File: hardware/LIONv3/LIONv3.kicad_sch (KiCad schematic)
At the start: 41 parts, among them SW1 RESET, SW2 BOOT, U1 TCAN3414DR, U14 UART, U15 I2C, U16 CAN, U17 PWR_3V3, U18 PWR_5V, U19 PWR_GND, U2 TYPE-C_16PIN_2MD(073), U3 ESP32-C6-MINI-1-N4, U4 TMP112AIDRLR

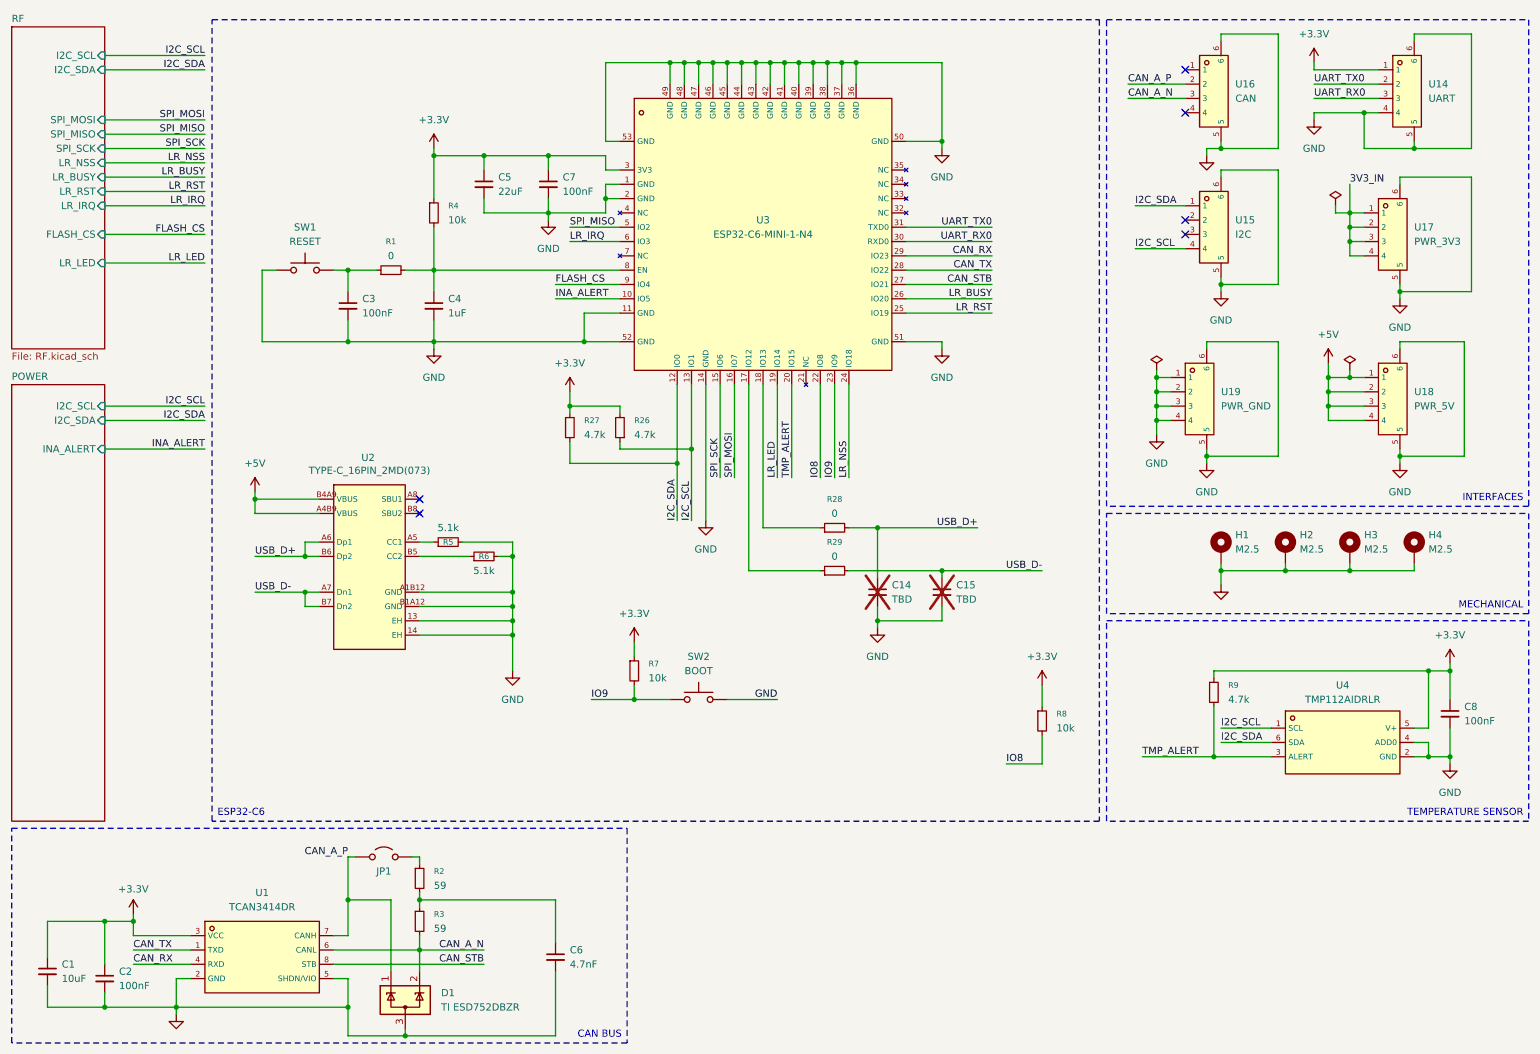
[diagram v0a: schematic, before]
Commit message: feat(hardware): add final components position
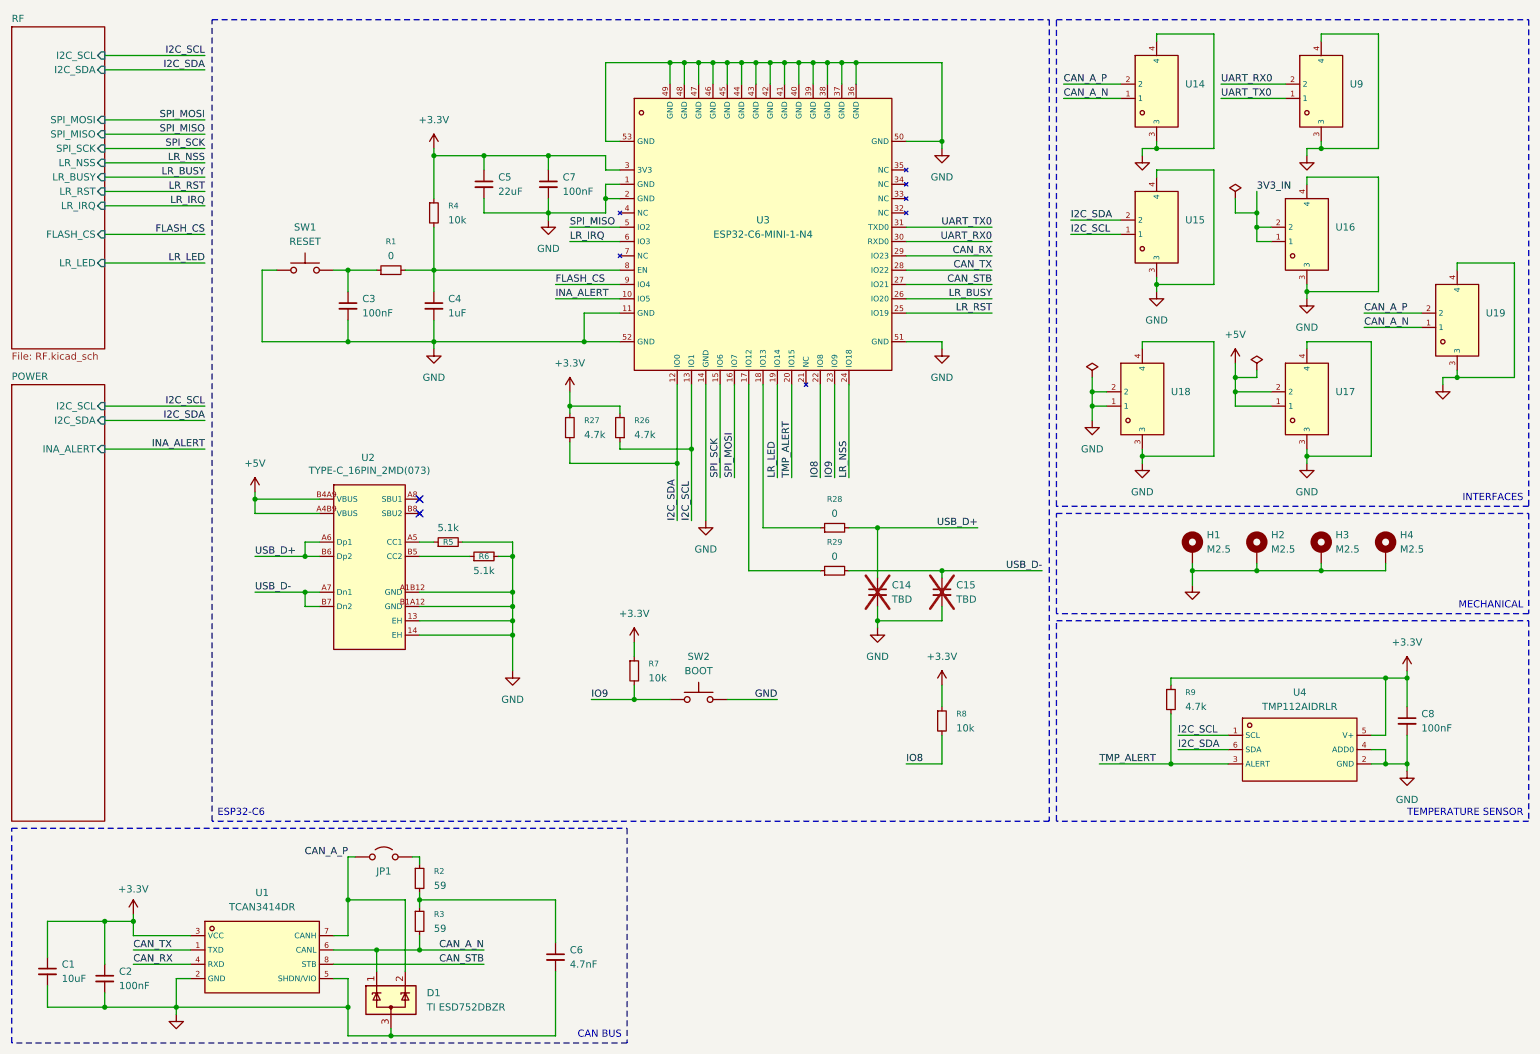
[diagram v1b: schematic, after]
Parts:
- removed U14: UART, LIONv3-Footprints:CONN-SMD_4P-P1.25_53261-0471, symbol LIONv3-Symbols:532610471_C696092
- removed U15: I2C, LIONv3-Footprints:CONN-SMD_4P-P1.25_53261-0471, symbol LIONv3-Symbols:532610471_C696092
- removed U16: CAN, LIONv3-Footprints:CONN-SMD_4P-P1.25_53261-0471, symbol LIONv3-Symbols:532610471_C696092
- removed U17: PWR_3V3, LIONv3-Footprints:CONN-SMD_4P-P1.25_53261-0471, symbol LIONv3-Symbols:532610471_C696092
- removed U18: PWR_5V, LIONv3-Footprints:CONN-SMD_4P-P1.25_53261-0471, symbol LIONv3-Symbols:532610471_C696092
- removed U19: PWR_GND, LIONv3-Footprints:CONN-SMD_4P-P1.25_53261-0471, symbol LIONv3-Symbols:532610471_C696092
- added U14, U15, U16, U17, U18, U19, U9: HC-1_25-2PWT, LIONv3-Footprints:CONN-SMD_2P-P1.25-HC-1.25-2PWT, symbol LIONv3-Symbols:HC-1_25-2PWT
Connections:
- net +5V: now also U17.1, U17.2
- net 3V3_IN: now also U16.1, U16.2
- net CAN_A_N: now also D1.1 (K), U14.1, U19.1; no longer D1.2 (K)
- net CAN_A_P: now also D1.2 (K), U14.2, U19.2; no longer D1.1 (K)
- net GND: now also U14.3, U14.4, U15.3, U15.4, U16.3, U16.4, U17.3, U17.4, U18.1, U18.2, U18.3, U18.4, U19.3, U19.4, U9.3, U9.4
- net I2C_SCL: now also U15.1
- net I2C_SDA: now also U15.2
- net UART_RX0: now also U9.2
- net UART_TX0: now also U9.1
- no-connect marks 6 -> 2
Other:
- moved on the sheet: C8, D1, H1, H2, H3, H4, R8, R9, U4

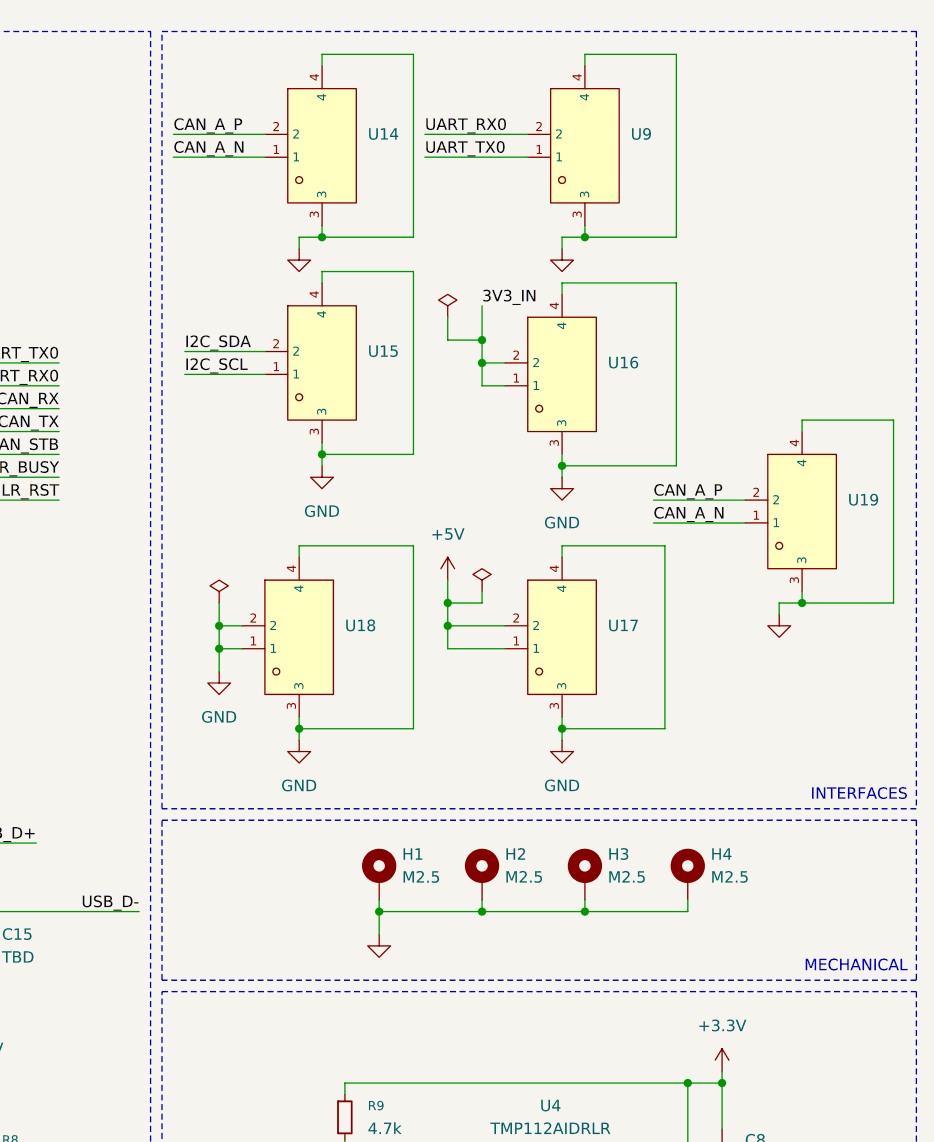
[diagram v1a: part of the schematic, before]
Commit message: feat(hardware): organize repo structure
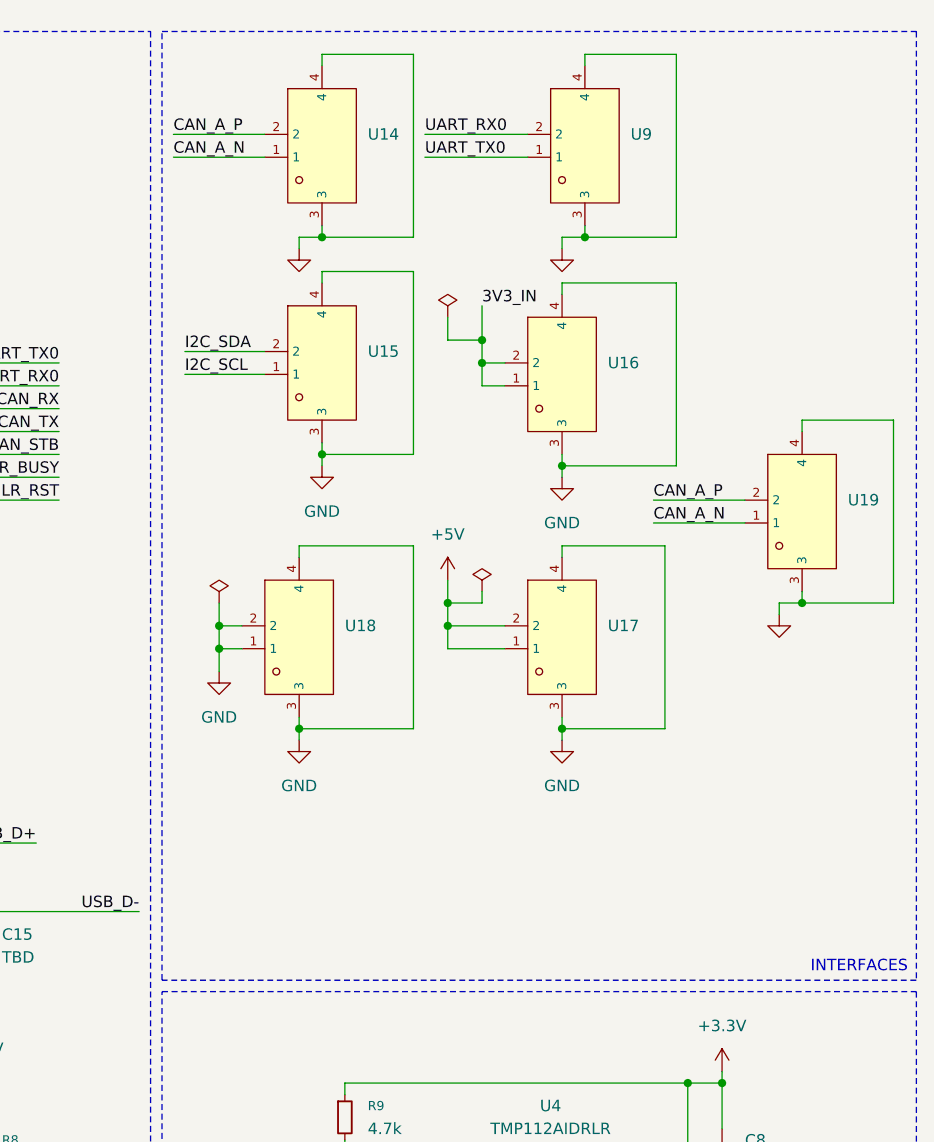
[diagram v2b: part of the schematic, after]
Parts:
- removed H1, H2, H3, H4: M2.5, MountingHole:MountingHole_2.5mm_Pad_Via, symbol Mechanical:MountingHole_Pad

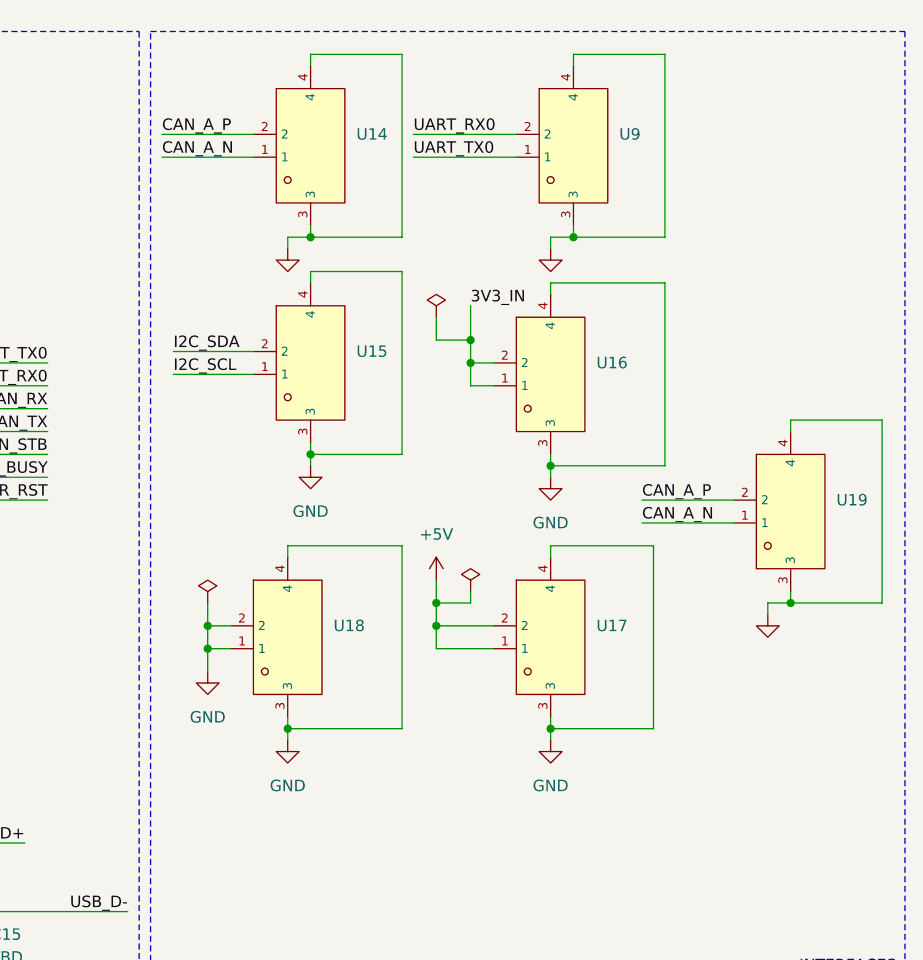
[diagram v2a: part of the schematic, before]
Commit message: feat(hardware): add power layout
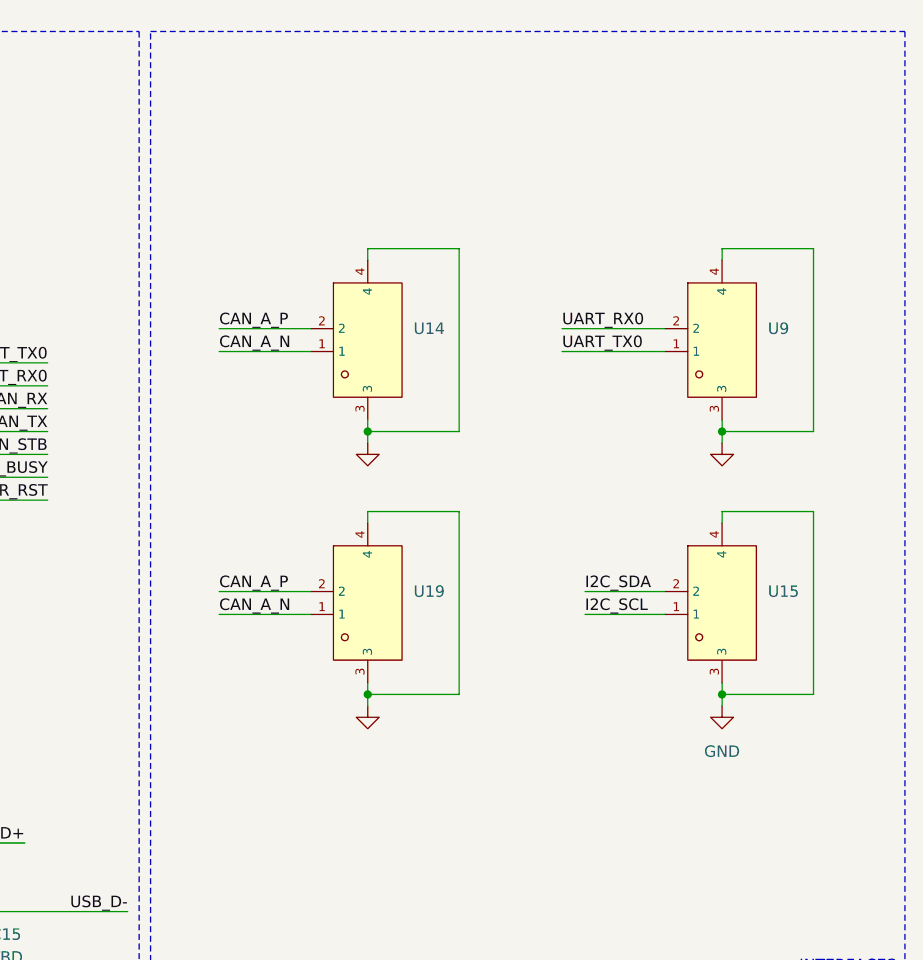
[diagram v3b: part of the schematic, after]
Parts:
- removed U16, U17, U18: HC-1_25-2PWT, LIONv3-Footprints:CONN-SMD_2P-P1.25-HC-1.25-2PWT, symbol LIONv3-Symbols:HC-1_25-2PWT
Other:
- moved on the sheet: U14, U15, U19, U9
